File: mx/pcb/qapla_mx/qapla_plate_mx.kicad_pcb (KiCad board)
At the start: 2 copper layers, 164.2 x 137.2 mm, 5 parts

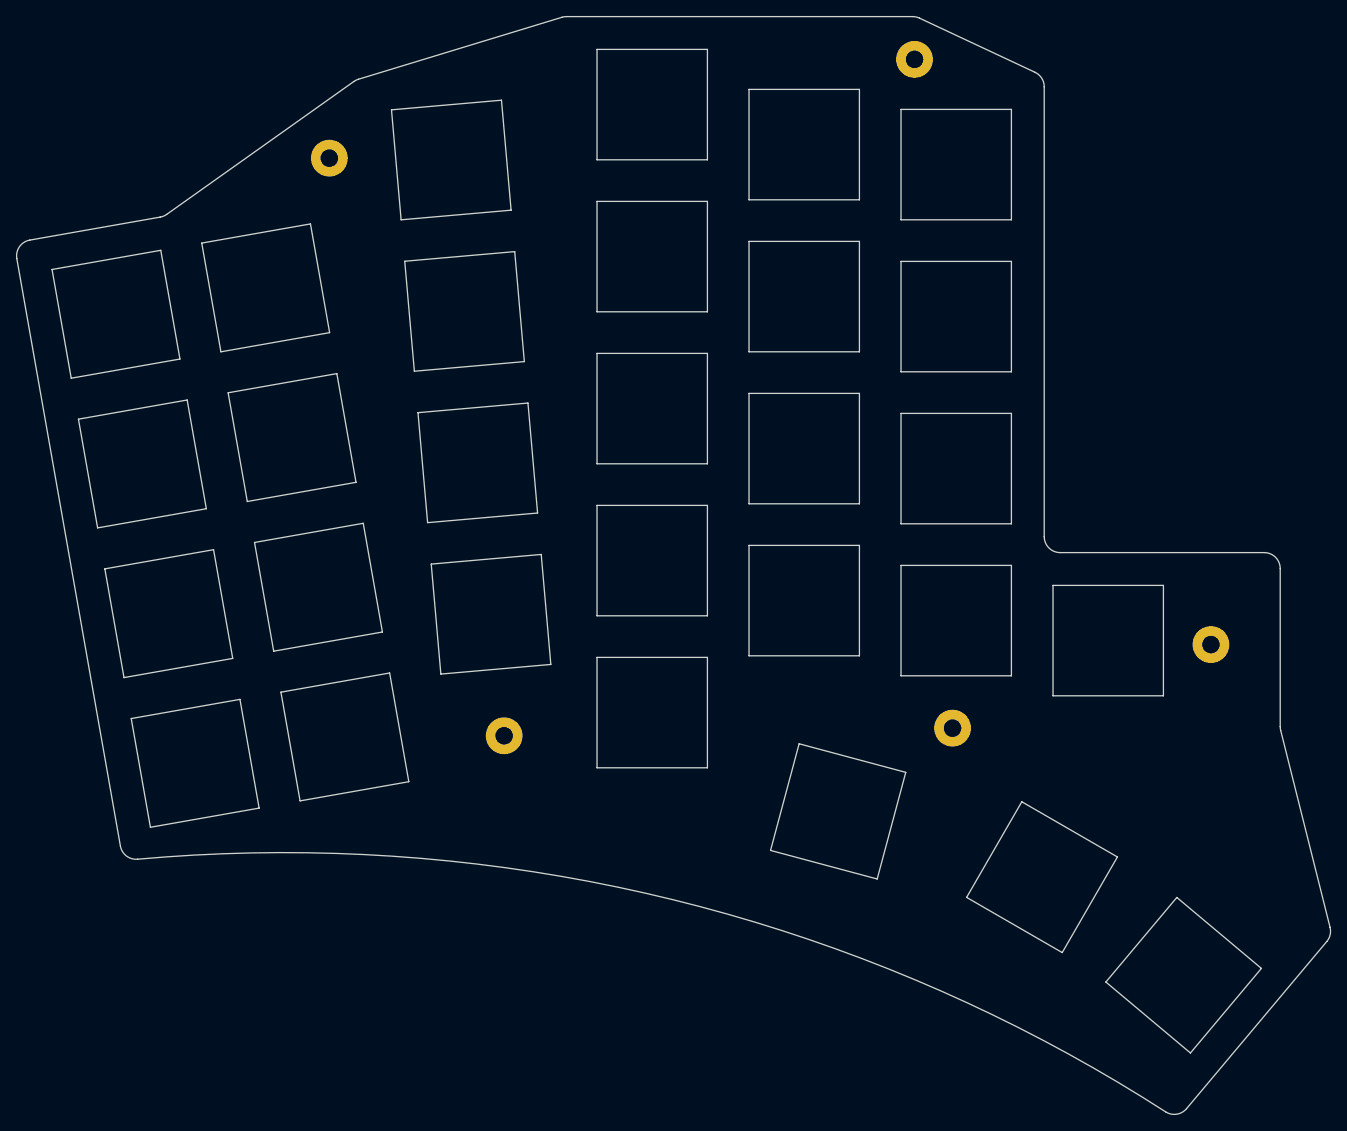
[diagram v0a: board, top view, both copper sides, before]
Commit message: Routing MX switches
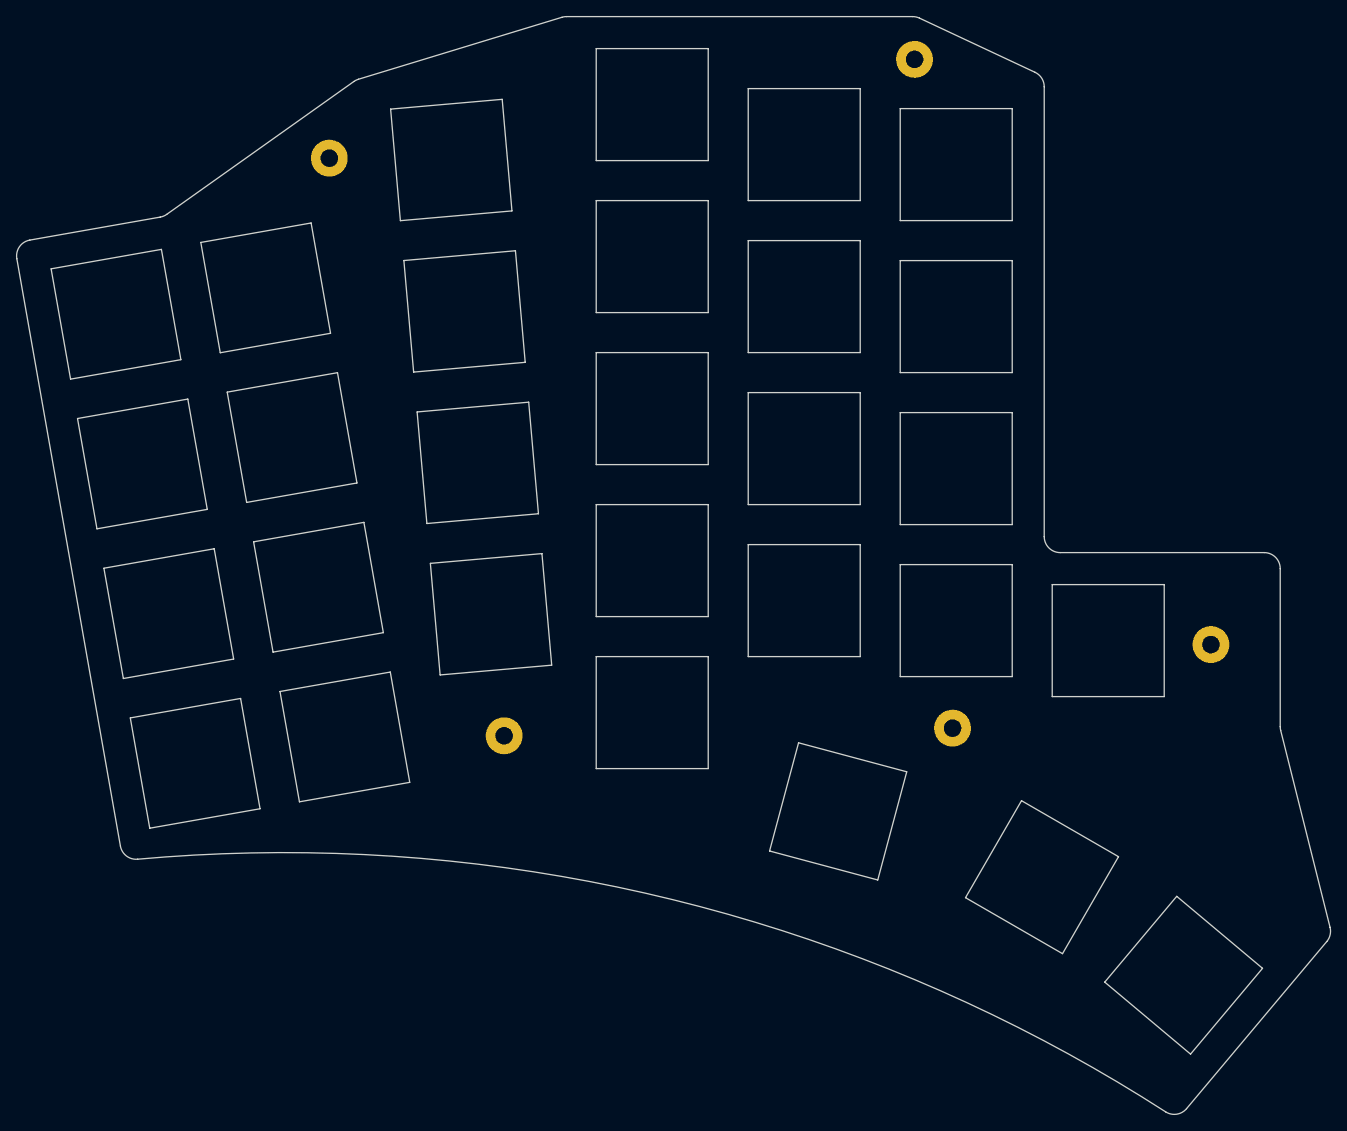
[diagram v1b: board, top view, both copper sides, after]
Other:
- outline, holes or cut-outs redrawn
